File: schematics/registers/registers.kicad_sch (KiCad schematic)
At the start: 72 parts, among them U1 74LS574, U2 74LS574, U3 74LS574, U4 74LS574, U5 74LS245, U6 74LS245, U7 74LS245, U8 74LS245

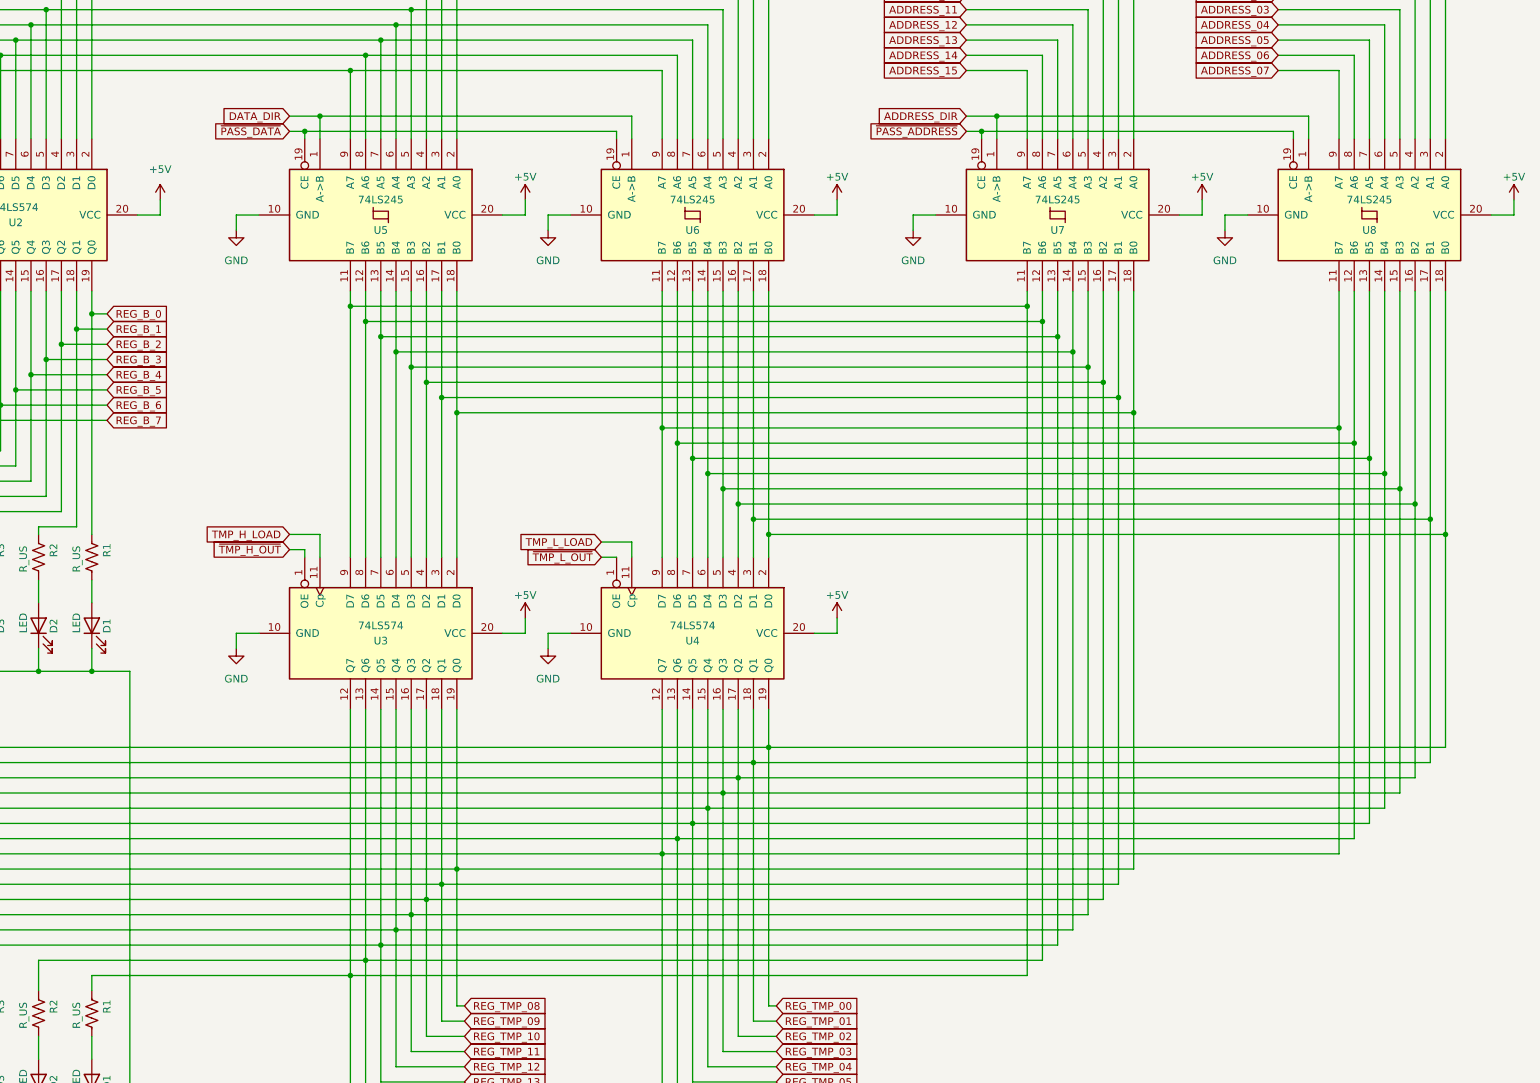
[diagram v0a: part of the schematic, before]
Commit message: Corrections after second diy pcb soldered
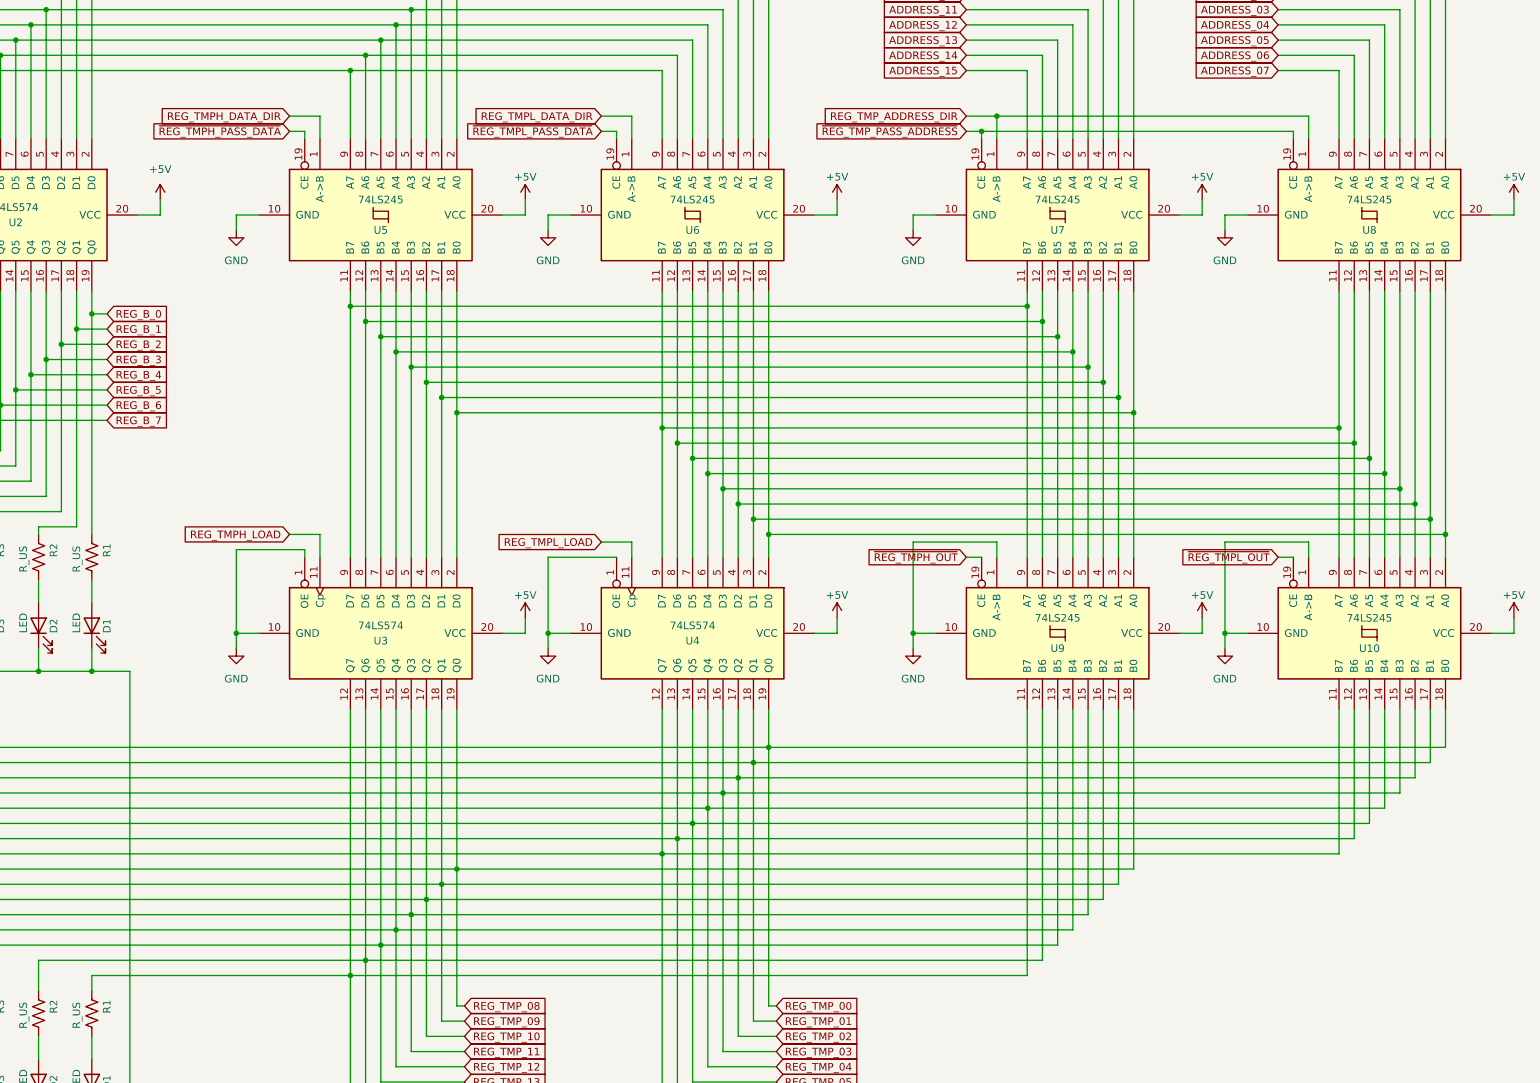
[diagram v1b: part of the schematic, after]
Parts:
- added U10, U9: 74LS245, symbol 74xx:74LS245
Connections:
- net ~{TMP_H_OUT} is gone; now on net GND: U3.1 (OE)
- net ~{TMP_L_OUT} is gone; now on net GND: U4.1 (OE)
- net +5V: now also U10.20 (VCC), U9.20 (VCC)
- net GND: now also U10.1 (A->B), U10.10 (GND), U9.1 (A->B), U9.10 (GND)
- net REG_TMP_00: now also U10.18 (B0); no longer U4.2 (D0), U6.18 (B0), U8.18 (B0)
- net REG_TMP_01: now also U10.17 (B1); no longer U4.3 (D1), U6.17 (B1), U8.17 (B1)
- net REG_TMP_02: now also U10.16 (B2); no longer U4.4 (D2), U6.16 (B2), U8.16 (B2)
- net REG_TMP_03: now also U10.15 (B3); no longer U4.5 (D3), U6.15 (B3), U8.15 (B3)
- net REG_TMP_04: now also U10.14 (B4); no longer U4.6 (D4), U6.14 (B4), U8.14 (B4)
- net REG_TMP_05: now also U10.13 (B5); no longer U4.7 (D5), U6.13 (B5), U8.13 (B5)
- net REG_TMP_06: now also U10.12 (B6); no longer U4.8 (D6), U6.12 (B6), U8.12 (B6)
- net REG_TMP_07: now also U10.11 (B7); no longer U4.9 (D7), U6.11 (B7), U8.11 (B7)
- net REG_TMP_08: now also U9.18 (B0); no longer U3.2 (D0), U5.18 (B0), U7.18 (B0)
- net REG_TMP_09: now also U9.17 (B1); no longer U3.3 (D1), U5.17 (B1), U7.17 (B1)
- net REG_TMP_10: now also U9.16 (B2); no longer U3.4 (D2), U5.16 (B2), U7.16 (B2)
- net REG_TMP_11: now also U9.15 (B3); no longer U3.5 (D3), U5.15 (B3), U7.15 (B3)
- net REG_TMP_12: now also U9.14 (B4); no longer U3.6 (D4), U5.14 (B4), U7.14 (B4)
- net REG_TMP_13: now also U9.13 (B5); no longer U3.7 (D5), U5.13 (B5), U7.13 (B5)
- net REG_TMP_14: now also U9.12 (B6); no longer U3.8 (D6), U5.12 (B6), U7.12 (B6)
- net REG_TMP_15: now also U9.11 (B7); no longer U3.9 (D7), U5.11 (B7), U7.11 (B7)
- net ADDRESS_DIR renamed REG_TMP_ADDRESS_DIR
- net DATA_DIR renamed REG_TMPH_DATA_DIR
- net REG_TMPH_DATA_DIR: no longer U6.1 (A->B)
- net TMP_H_LOAD renamed REG_TMPH_LOAD
- net TMP_L_LOAD renamed REG_TMPL_LOAD
- net ~{PASS_ADDRESS} renamed ~{REG_TMP_PASS_ADDRESS}
- net ~{PASS_DATA} renamed ~{REG_TMPH_PASS_DATA}
- net ~{REG_TMPH_PASS_DATA}: no longer U6.19 (CE)
- new net: U10.9 (A7), U4.9 (D7), U6.11 (B7), U8.11 (B7)
- new net: U10.8 (A6), U4.8 (D6), U6.12 (B6), U8.12 (B6)
- new net: U10.7 (A5), U4.7 (D5), U6.13 (B5), U8.13 (B5)
- new net: U10.6 (A4), U4.6 (D4), U6.14 (B4), U8.14 (B4)
- new net: U10.5 (A3), U4.5 (D3), U6.15 (B3), U8.15 (B3)
- new net: U10.4 (A2), U4.4 (D2), U6.16 (B2), U8.16 (B2)
- new net: U10.3 (A1), U4.3 (D1), U6.17 (B1), U8.17 (B1)
- new net: U10.2 (A0), U4.2 (D0), U6.18 (B0), U8.18 (B0)
- new net: U3.9 (D7), U5.11 (B7), U7.11 (B7), U9.9 (A7)
- new net: U3.8 (D6), U5.12 (B6), U7.12 (B6), U9.8 (A6)
- new net: U3.7 (D5), U5.13 (B5), U7.13 (B5), U9.7 (A5)
- new net: U3.6 (D4), U5.14 (B4), U7.14 (B4), U9.6 (A4)
- new net: U3.5 (D3), U5.15 (B3), U7.15 (B3), U9.5 (A3)
- new net: U3.4 (D2), U5.16 (B2), U7.16 (B2), U9.4 (A2)
- new net: U3.3 (D1), U5.17 (B1), U7.17 (B1), U9.3 (A1)
- new net: U3.2 (D0), U5.18 (B0), U7.18 (B0), U9.2 (A0)
- new net REG_TMPL_DATA_DIR: U6.1 (A->B)
- new net ~{REG_TMPH_OUT}: U9.19 (CE)
- new net ~{REG_TMPL_OUT}: U10.19 (CE)
- new net ~{REG_TMPL_PASS_DATA}: U6.19 (CE)
